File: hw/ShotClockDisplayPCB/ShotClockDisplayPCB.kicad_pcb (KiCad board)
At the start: 4 copper layers, 54.5 x 54 mm, 19 parts, among them J1 Conn_01x02_Pin, J2 Conn_01x02_Pin, J3 Conn_01x02_Pin, J4 Conn_01x02_Pin, J5 Conn_01x05_Socket, J6 Conn_01x05_Socket, J7 Conn_01x05_Socket, J8 Conn_01x05_Socket, U1 S6B-PH-K-S-(LF)(SN), U2 TLC59116IRHBR

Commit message: Fixed mainboard with feedback from Luc
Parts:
- moved J4 34.5 mm to (42.9, 54.5), turned to 180 degrees
- moved J3 25.9 mm to (42.9, 47.8), turned to 180 degrees
- moved J1 17.4 mm to (42.4, 35.0), turned to 180 degrees
- moved J2 7.98 mm to (42.6, 41.0), turned to 180 degrees
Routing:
- net SEG1_G: track 41.7 -> 48.2 mm
- net /I2C PWM IO Expander/A0: track 38.2 -> 31.8 mm
- net SEG1_F: track 38.2 -> 42.5 mm
- net /I2C PWM IO Expander/A1: track 24.8 -> 22.3 mm
- removed copper zone on B.Cu, net +5V

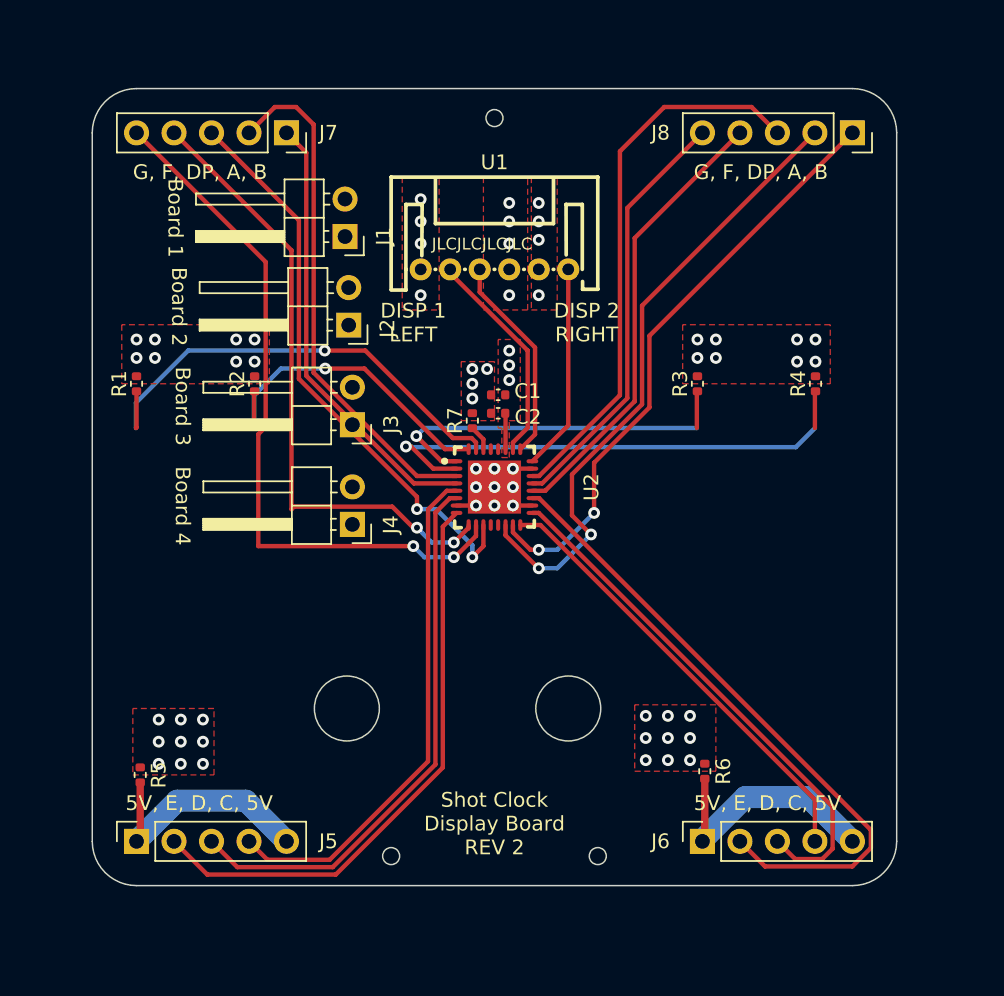
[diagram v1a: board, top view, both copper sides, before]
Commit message: Rerouted display board
And added GND planes everywhere, created step file
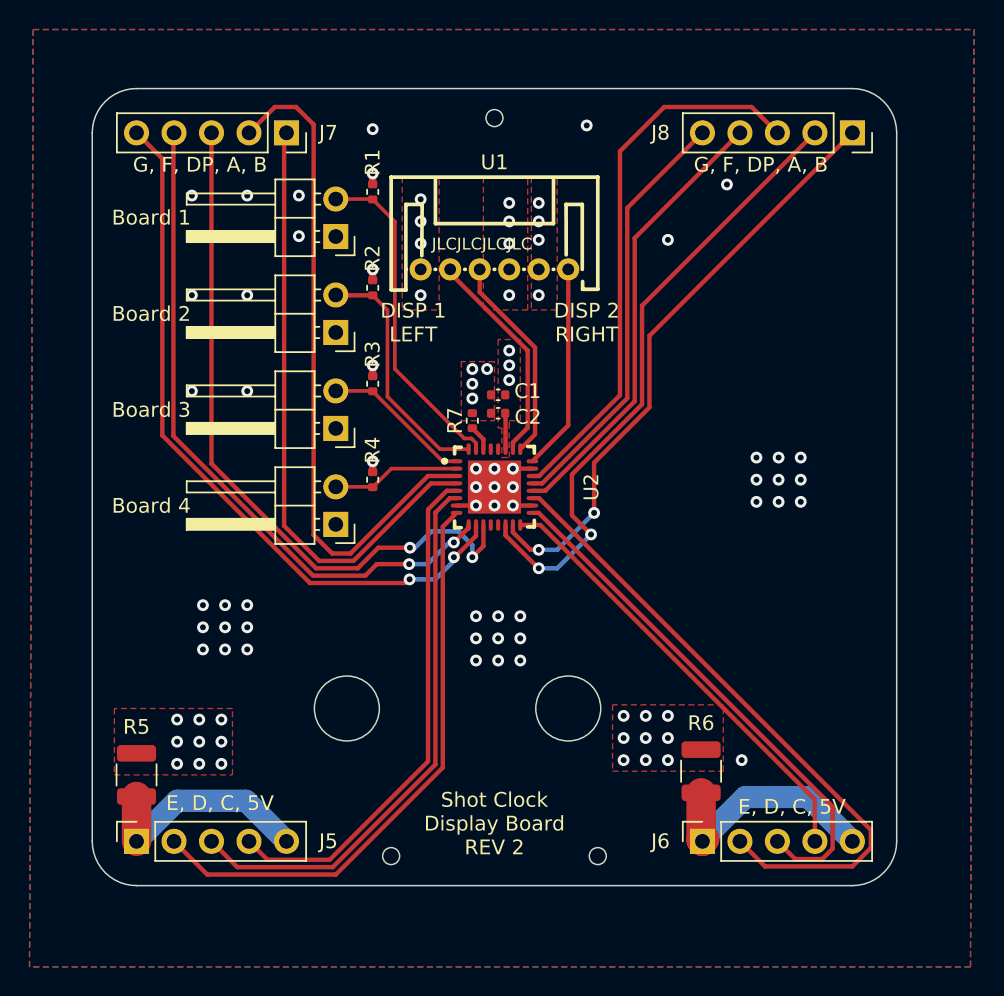
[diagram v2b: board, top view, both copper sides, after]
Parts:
- R5, R6: footprint Resistor_SMD:R_0402_1005Metric -> Resistor_SMD:R_1210_3225Metric
- moved R4 30.7 mm to (44.2, 51.5)
- moved R3 22.0 mm to (44.2, 45.0)
- moved R1 20.6 mm to (44.2, 32.0)
- moved R2 10.3 mm to (44.2, 38.5)
- moved J3 1.15 mm to (41.8, 48.0)
- moved J4 1.12 mm to (41.8, 54.5)
- moved J2 1.01 mm to (41.8, 41.5)
- moved J1 0.62 mm to (41.8, 35.0)
- moved R5 0.25 mm to (28.2, 71.5)
- moved R6 0.25 mm to (66.5, 71.2)
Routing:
- net /I2C PWM IO Expander/A3: track 34.8 -> 8.71 mm, vias 1 -> 0
- net /I2C PWM IO Expander/A2: track 25.2 -> 10.2 mm, vias 1 -> 0
- net SEG1_B: track 30.2 -> 41.5 mm
- net SEG1_A: track 35.0 -> 45.8 mm
- net /I2C PWM IO Expander/A0: track 31.8 -> 22.6 mm, vias 1 -> 0
- net SEG1_DP: track 39.3 -> 47.9 mm
- net /I2C PWM IO Expander/A1: track 22.3 -> 16.8 mm, vias 1 -> 0
- net SEG1_F: track 42.5 -> 46.0 mm
- net GND: track 3.96 -> 6.92 mm, vias 33 -> 67
- net /Segment Display Connectors/5V_CONN2: track 17.0 -> 16.3 mm
- net /Segment Display Connectors/5V_CONN1: track 16.5 -> 15.8 mm
- net SEG1_G: track 48.2 -> 48.8 mm
- added copper zone on In2.Cu, net +5V
- added copper zone on B.Cu, net GND
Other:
- board text added: "E, D, C, 5V"
- board text removed: "5V, E, D, C, 5V"

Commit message: REV2 Finished
Corrected LCSC part number
Added polarities on silkscreen
Made output files for both boards
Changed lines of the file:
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@@
       (outputformat 1)
       (mirror false)
-      (drillshape 1)
+      (drillshape 0)
       (scaleselection 1)
-      (outputdirectory "")
+      (outputdirectory "output/mftr/gerber/rev2/")
     )
   )
@@
     (fp_line (start 1.6 1.245) (end -1.6 1.245)
       (stroke (width 0.1) (type solid)) (layer "F.Fab"))
-    (pad "1" smd roundrect (at -1.4625 0 270) (size 1.125 2.65) (layers "F.Cu" "F.Paste" "F.Mask") (roundrect_rratio 0.222222)
+    (pad "1" smd roundrect (at -1.4625 0 270) (size 1.125 2.65) (layers "F.Cu" "F.Paste" "F.Mask") (roundrect_rratio 0.2222222222)
       (net 1 "+5V") (pintype "passive"))
-    (pad "2" smd roundrect (at 1.4625 0 270) (size 1.125 2.65) (layers "F.Cu" "F.Paste" "F.Mask") (roundrect_rratio 0.222222)
+    (pad "2" smd roundrect (at 1.4625 0 270) (size 1.125 2.65) (layers "F.Cu" "F.Paste" "F.Mask") (roundrect_rratio 0.2222222222)
       (net 33 "/Segment Display Connectors/5V_CONN2") (pintype "passive"))
     (model "${KICAD6_3DMODEL_DIR}/Resistor_SMD.3dshapes/R_1210_3225Metric.wrl"
@@
     (fp_line (start 1.6 1.245) (end -1.6 1.245)
       (stroke (width 0.1) (type solid)) (layer "F.Fab"))
-    (pad "1" smd roundrect (at -1.4625 0 270) (size 1.125 2.65) (layers "F.Cu" "F.Paste" "F.Mask") (roundrect_rratio 0.222222)
+    (pad "1" smd roundrect (at -1.4625 0 270) (size 1.125 2.65) (layers "F.Cu" "F.Paste" "F.Mask") (roundrect_rratio 0.2222222222)
       (net 1 "+5V") (pintype "passive"))
-    (pad "2" smd roundrect (at 1.4625 0 270) (size 1.125 2.65) (layers "F.Cu" "F.Paste" "F.Mask") (roundrect_rratio 0.222222)
+    (pad "2" smd roundrect (at 1.4625 0 270) (size 1.125 2.65) (layers "F.Cu" "F.Paste" "F.Mask") (roundrect_rratio 0.2222222222)
       (net 32 "/Segment Display Connectors/5V_CONN1") (pintype "passive"))
     (model "${KICAD6_3DMODEL_DIR}/Resistor_SMD.3dshapes/R_1210_3225Metric.wrl"
